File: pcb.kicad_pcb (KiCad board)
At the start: 2 copper layers, 247.4 x 97.8 mm, 194 parts, among them J0 USB_mini_micro_B, P1 CONN_01X06, P2 CONN_01X04, P3 CONN_01X03, P4 CONN_01X02, SW1.1 Backtick, SW1.10 9, SW1.11 0, SW1.12 -, SW1.13 =, SW1.2 1, SW1.3 2, SW1.4 3, SW1.5 4, SW1.6 5, SW1.7 6, SW1.8 7, SW1.9 8, SW2.1 Tab, SW2.10 I, SW2.11 O, SW2.12 P, SW2.13 /, SW2.2 Q, SW2.3 W, SW2.4 E, SW2.5 R, SW2.6 T, SW2.8 Y, SW2.9 U, SW3.1 Bksp, SW3.10 K, SW3.11 L, SW3.12 ;, SW3.13 Enter, SW3.2 A, SW3.3 S, SW3.4 D, SW3.5 F, SW3.6 G, SW3.8 H, SW3.9 J, SW4.10 ,, SW4.11 ., SW4.12 ., SW4.2 Z, SW4.3 Z, SW4.4 X, SW4.5 C, SW4.6 V, SW4.7 H, SW4.8 N, SW4.9 M, SW4A1 LShift, SW4A13 RShift, SW4B1 LShift, SW4B13 RShift, SW5A1 1.5, SW5A10 1.5, SW5A12 1.5, SW5A13 1.5, SW5A2 LGUI, SW5A4 LAlt, SW5A7 2.25, SW5A9 2.75, SW5B1 LCtrl, SW5B10 1, SW5B11 1, SW5B12 1, SW5B13 1, SW5B2 LGUI, SW5B3 1, SW5B4 LAlt, SW5B7 2.75, SW5B9 2.25, SW5C5 1.5, SW5C7 2/3, SW5C9 1.5, SW5D5 1, SW5D9 1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

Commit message: Added labeling to R5 stabs.
Added A, B, C labels to stabilizer holes and associated switch holes.
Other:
- board text added: "7A"
- board text added: "7B"
- board text added: "7C"
- board text added: "9A"
- board text added: "9B"
- board text added: "A"
- board text added: "B"
- board text added: "C"
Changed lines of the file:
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@@
     (area 76.251999 89.078999 323.798001 187.019001)
     (thickness 1.6)
-    (drawings 213)
+    (drawings 223)
     (tracks 1410)
     (zones 0)
@@
       (xy -0.381 3.8735) (xy -0.379184 2.428875)) (layer B.SilkS) (width 0.01))
   )
+  (gr_text A (at 159.131 184.404) (layer B.SilkS)
+    (effects (font (size 1 1) (thickness 0.25)) (justify mirror))
+  )
+  (gr_text B (at 169.418 184.404) (layer B.SilkS)
+    (effects (font (size 1 1) (thickness 0.25)) (justify mirror))
+  )
+  (gr_text A (at 183.007 184.404) (layer B.SilkS)
+    (effects (font (size 1 1) (thickness 0.25)) (justify mirror))
+  )
+  (gr_text B (at 193.294 184.404) (layer B.SilkS)
+    (effects (font (size 1 1) (thickness 0.25)) (justify mirror))
+  )
+  (gr_text C (at 188.087 181.61) (layer B.SilkS)
+    (effects (font (size 1 1) (thickness 0.25)) (justify mirror))
+  )
+  (gr_text C (at 211.963 181.61) (layer B.SilkS)
+    (effects (font (size 1 1) (thickness 0.25)) (justify mirror))
+  )
+  (gr_text A (at 206.756 184.404) (layer B.SilkS)
+    (effects (font (size 1 1) (thickness 0.25)) (justify mirror))
+  )
+  (gr_text B (at 217.043 184.404) (layer B.SilkS)
+    (effects (font (size 1 1) (thickness 0.25)) (justify mirror))
+  )
+  (gr_text A (at 230.632 184.404) (layer B.SilkS)
+    (effects (font (size 1 1) (thickness 0.25)) (justify mirror))
+  )
+  (gr_text B (at 240.919 184.404) (layer B.SilkS)
+    (effects (font (size 1 1) (thickness 0.25)) (justify mirror))
+  )
   (gr_line (start 225.552 107.188) (end 225.298 107.442) (angle 90) (layer B.SilkS) (width 0.2))
   (gr_line (start 225.298 106.934) (end 225.552 107.188) (angle 90) (layer B.SilkS) (width 0.2))
@@
     (effects (font (size 1 1) (thickness 0.25)) (justify mirror))
   )
-  (gr_text 9 (at 226.21875 179.59375) (layer B.SilkS)
+  (gr_text 9B (at 226.21875 179.59375) (layer B.SilkS)
     (effects (font (size 1 1) (thickness 0.25)) (justify mirror))
   )
-  (gr_text 9 (at 221.45625 179.59375) (layer B.SilkS)
+  (gr_text 9A (at 221.45625 179.59375) (layer B.SilkS)
     (effects (font (size 1 1) (thickness 0.25)) (justify mirror))
   )
@@
     (effects (font (size 1 1) (thickness 0.25)) (justify mirror))
   )
-  (gr_text 7 (at 200.025 179.59375) (layer B.SilkS)
+  (gr_text 7C (at 200.025 179.59375) (layer B.SilkS)
     (effects (font (size 1 1) (thickness 0.25)) (justify mirror))
   )
-  (gr_text 7 (at 178.59375 179.59375) (layer B.SilkS)
+  (gr_text 7B (at 178.59375 179.59375) (layer B.SilkS)
     (effects (font (size 1 1) (thickness 0.25)) (justify mirror))
   )
-  (gr_text 7 (at 173.83125 179.59375) (layer B.SilkS)
+  (gr_text 7A (at 173.83125 179.59375) (layer B.SilkS)
     (effects (font (size 1 1) (thickness 0.25)) (justify mirror))
   )

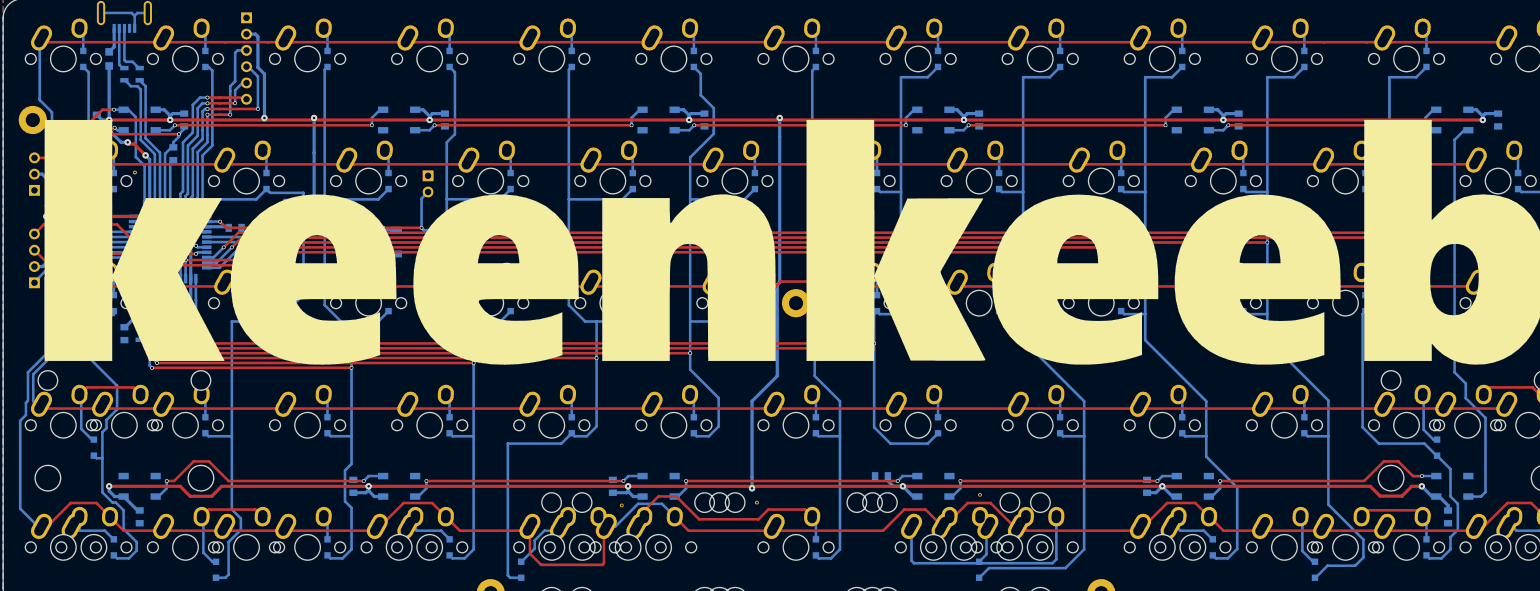
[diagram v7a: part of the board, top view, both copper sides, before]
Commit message: Cleaned up
Automerged traces and removed redundant holes.
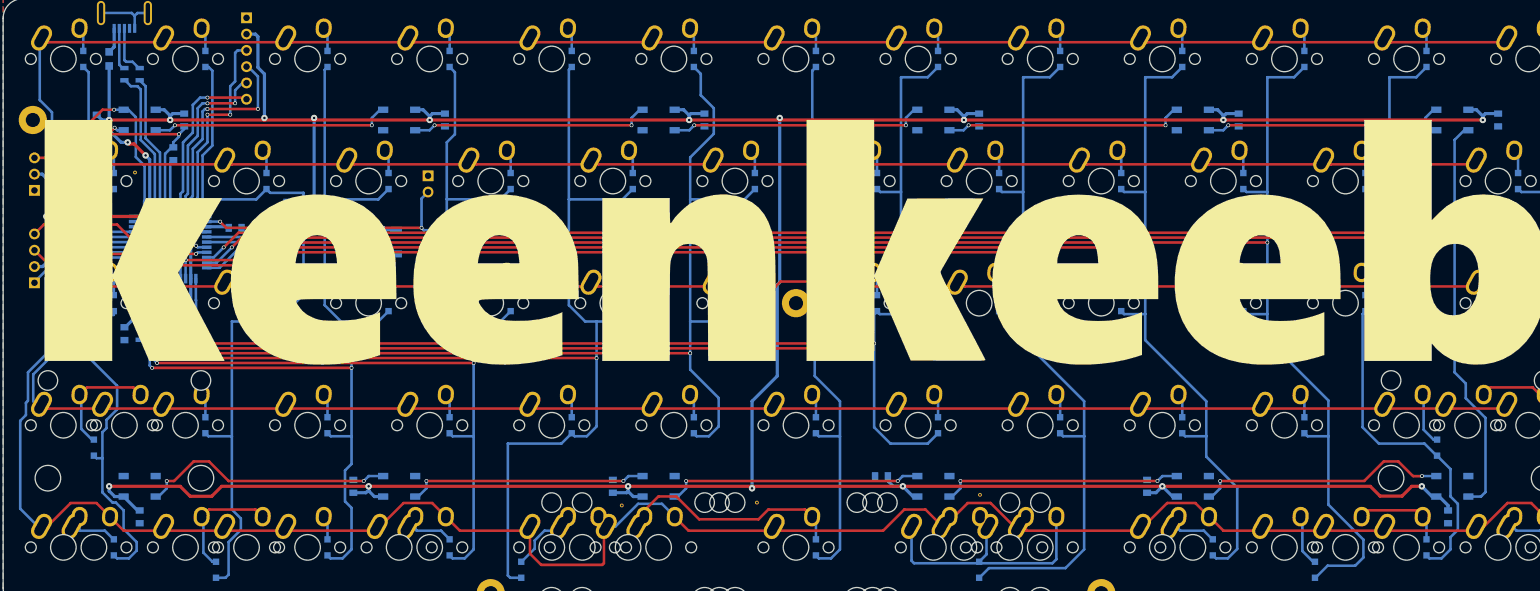
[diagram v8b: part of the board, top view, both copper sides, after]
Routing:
- net /matrix/Row5: track 332.7 -> 332.2 mm
